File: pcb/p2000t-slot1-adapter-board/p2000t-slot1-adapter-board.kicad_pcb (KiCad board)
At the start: 2 copper layers, 88.1 x 24.9 mm, 3 parts, among them J1 input, J2 P2000T_cartridge_edge

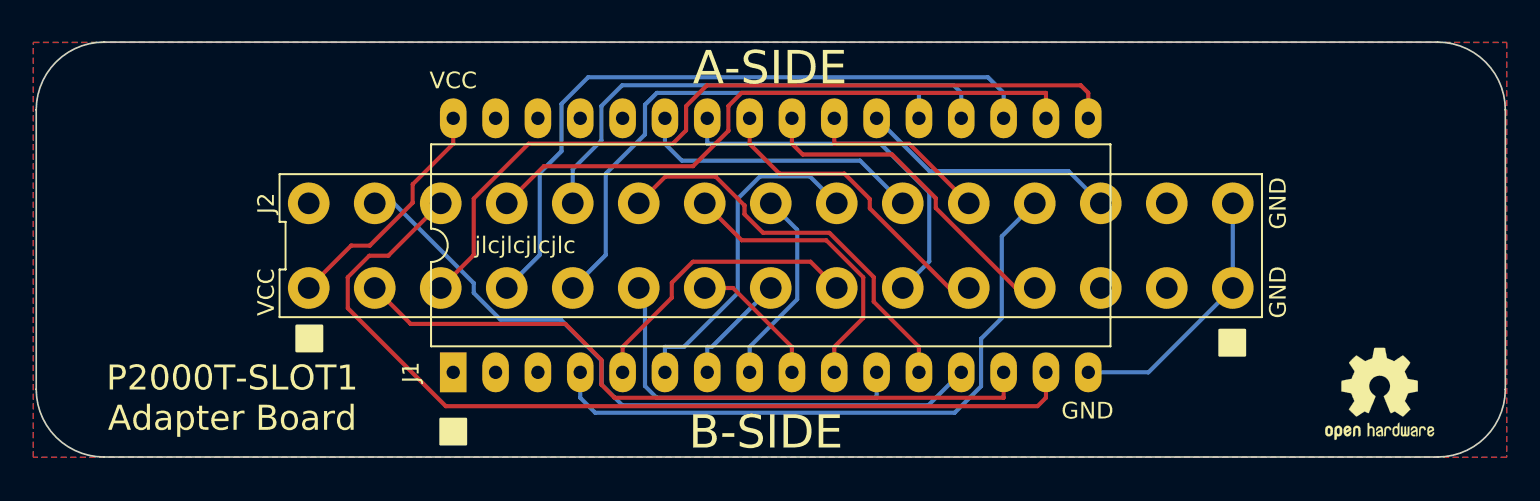
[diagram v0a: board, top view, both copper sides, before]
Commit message: Revising P2000T adapter board to accomodate ZIF lever
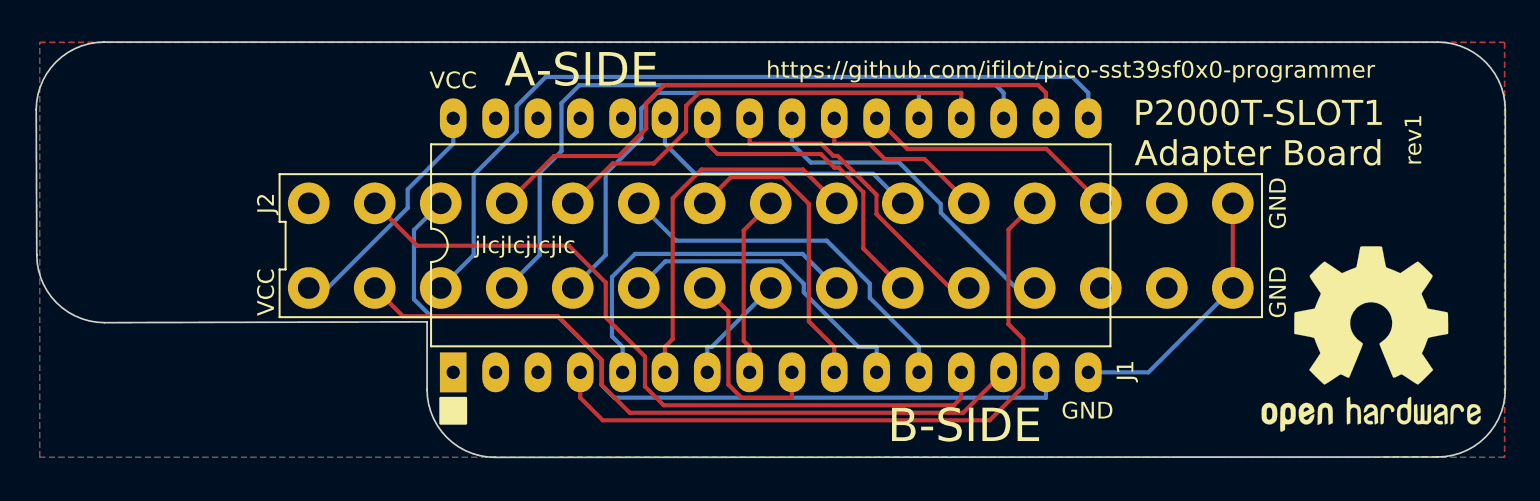
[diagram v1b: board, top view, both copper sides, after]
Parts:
- removed the REF** at (96.0, 38.9)
- added REF**: OSHW-Logo2_14.6x12mm_SilkScreen, Symbol:OSHW-Logo2_14.6x12mm_SilkScreen, F.Cu at (95.5, 35.6)
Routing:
- net D2: track 55.3 -> 49.2 mm
- net A3: track 8.22 -> 12.0 mm
- net A9: track 22.4 -> 18.8 mm
- net A7: track 17.7 -> 20.9 mm
- net A1: track 21.7 -> 18.9 mm
- net A12: track 38.9 -> 41.5 mm
- net A0: track 24.4 -> 22.4 mm
- net D0: track 42.2 -> 44.2 mm
- net A6: track 20.1 -> 22.0 mm
- net D6: track 30.4 -> 28.5 mm
- net D3: track 48.4 -> 49.7 mm
- net A4: track 12.0 -> 11.0 mm
- net A2: track 17.8 -> 18.3 mm
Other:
- outline, holes or cut-outs redrawn
- board text added: "https://github.com/ifilot/pico-sst39sf0x0-programmer"
- board text added: "rev1"
